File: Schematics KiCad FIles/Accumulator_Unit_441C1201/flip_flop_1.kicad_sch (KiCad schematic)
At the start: 13 parts, among them U1201 5963

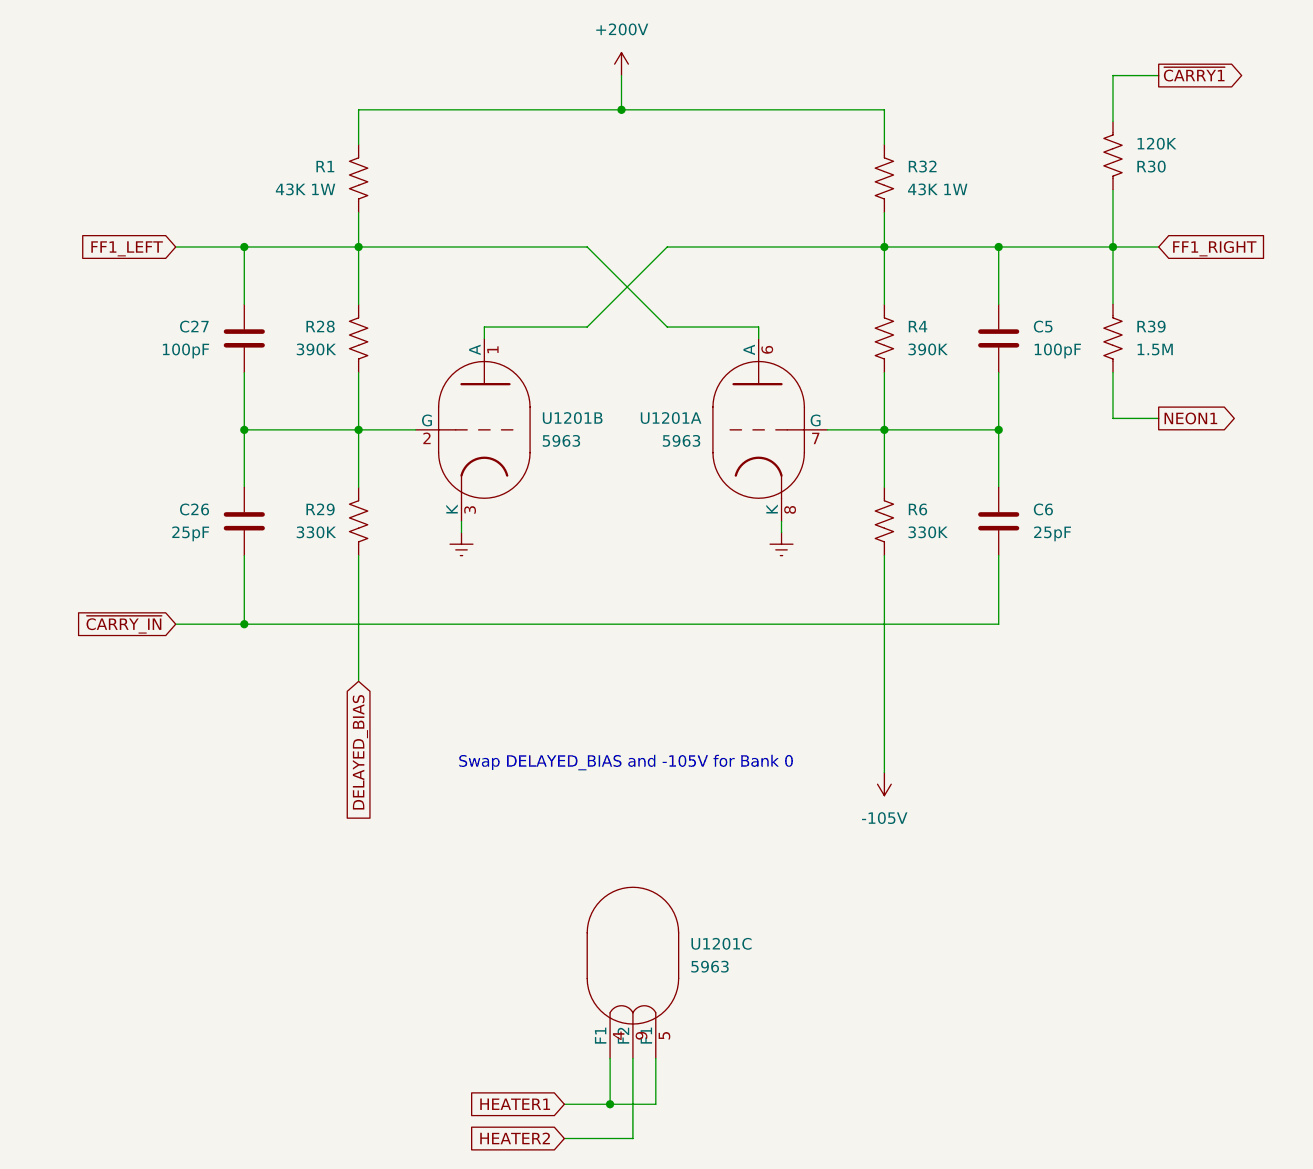
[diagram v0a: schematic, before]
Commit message: Fix component designators on accumulator schematics
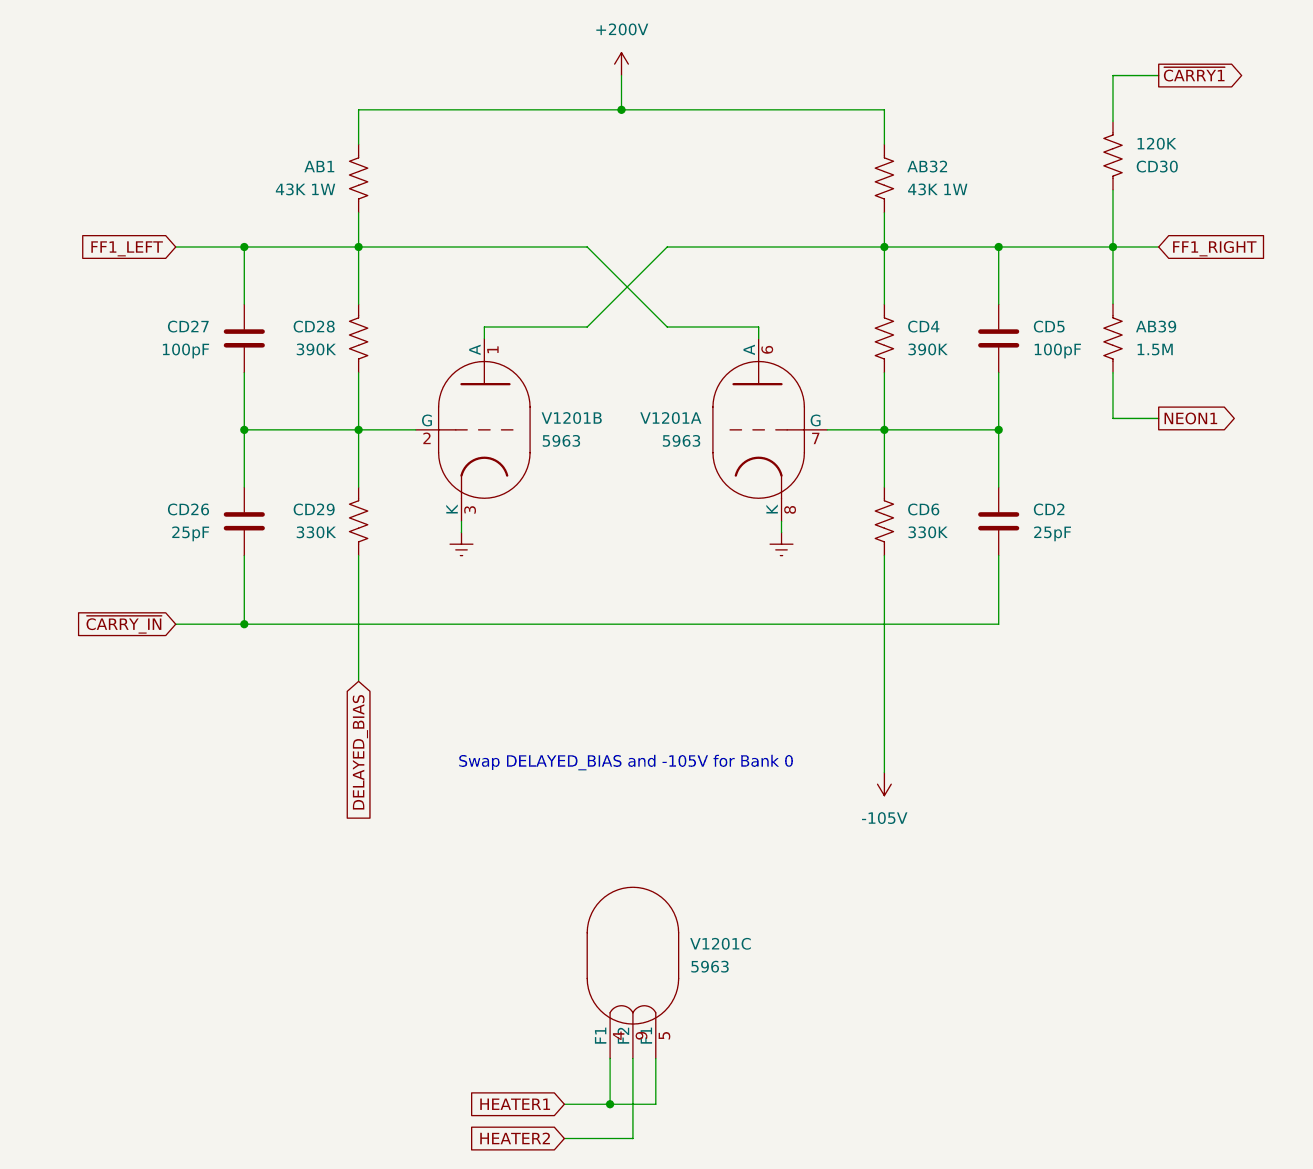
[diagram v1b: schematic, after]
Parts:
- renumbered R1 to AB1, R32 to AB32, R39 to AB39, C6 to CD2, C26 to CD26, C27 to CD27, R28 to CD28, R29 to CD29, R30 to CD30, R4 to CD4, C5 to CD5, R6 to CD6, U1201 to V1201
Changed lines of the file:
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@@
 		(on_board yes)
 		(dnp no)
-		(property "Reference" "R6"
+		(property "Reference" "CD6"
 			(at 171.45 85.0899 0)
 			(effects
@@
 			(project "Accumulator_Unit_441C1201"
 				(path "/519d7692-6bf3-45ab-bd58-713783b63e8a/fb897285-36a2-4bc7-a001-c032ab62393f"
-					(reference "R6")
+					(reference "CD6")
 					(unit 1)
 				)
@@
 		(on_board yes)
 		(dnp no)
-		(property "Reference" "R4"
+		(property "Reference" "CD4"
 			(at 171.45 64.7699 0)
 			(effects
@@
 			(project "Accumulator_Unit_441C1201"
 				(path "/519d7692-6bf3-45ab-bd58-713783b63e8a/fb897285-36a2-4bc7-a001-c032ab62393f"
-					(reference "R4")
+					(reference "CD4")
 					(unit 1)
 				)
@@
 		(on_board yes)
 		(dnp no)
-		(property "Reference" "R29"
+		(property "Reference" "CD29"
 			(at 107.95 85.0899 0)
 			(effects
@@
 			(project "Accumulator_Unit_441C1201"
 				(path "/519d7692-6bf3-45ab-bd58-713783b63e8a/fb897285-36a2-4bc7-a001-c032ab62393f"
-					(reference "R29")
+					(reference "CD29")
 					(unit 1)
 				)
@@
 		(on_board yes)
 		(dnp no)
-		(property "Reference" "U1201"
+		(property "Reference" "V1201"
 			(at 148.59 74.9299 0)
 			(effects
@@
 			(project "Accumulator_Unit_441C1201"
 				(path "/519d7692-6bf3-45ab-bd58-713783b63e8a/fb897285-36a2-4bc7-a001-c032ab62393f"
-					(reference "U1201")
+					(reference "V1201")
 					(unit 1)
 				)
@@
 		(on_board yes)
 		(dnp no)
-		(property "Reference" "C26"
+		(property "Reference" "CD26"
 			(at 93.98 85.0899 0)
 			(effects
@@
 			(project "Accumulator_Unit_441C1201"
 				(path "/519d7692-6bf3-45ab-bd58-713783b63e8a/fb897285-36a2-4bc7-a001-c032ab62393f"
-					(reference "C26")
+					(reference "CD26")
 					(unit 1)
 				)
@@
 		(on_board yes)
 		(dnp no)
-		(property "Reference" "R28"
+		(property "Reference" "CD28"
 			(at 107.95 64.7699 0)
 			(effects
@@
 			(project "Accumulator_Unit_441C1201"
 				(path "/519d7692-6bf3-45ab-bd58-713783b63e8a/fb897285-36a2-4bc7-a001-c032ab62393f"
-					(reference "R28")
+					(reference "CD28")
 					(unit 1)
 				)
@@
 		(on_board yes)
 		(dnp no)
-		(property "Reference" "R32"
+		(property "Reference" "AB32"
 			(at 171.45 46.9899 0)
 			(effects
@@
 			(project "Accumulator_Unit_441C1201"
 				(path "/519d7692-6bf3-45ab-bd58-713783b63e8a/fb897285-36a2-4bc7-a001-c032ab62393f"
-					(reference "R32")
+					(reference "AB32")
 					(unit 1)
 				)
@@
 		(dnp no)
 		(fields_autoplaced yes)
-		(property "Reference" "U1201"
+		(property "Reference" "V1201"
 			(at 147.32 133.3499 0)
 			(effects
@@
 			(project "Accumulator_Unit_441C1201"
 				(path "/519d7692-6bf3-45ab-bd58-713783b63e8a/fb897285-36a2-4bc7-a001-c032ab62393f"
-					(reference "U1201")
+					(reference "V1201")
 					(unit 3)
 				)
@@
 		(on_board yes)
 		(dnp no)
-		(property "Reference" "C5"
+		(property "Reference" "CD5"
 			(at 185.42 64.7699 0)
 			(effects
@@
 			(project "Accumulator_Unit_441C1201"
 				(path "/519d7692-6bf3-45ab-bd58-713783b63e8a/fb897285-36a2-4bc7-a001-c032ab62393f"
-					(reference "C5")
+					(reference "CD5")
 					(unit 1)
 				)
@@
 		(on_board yes)
 		(dnp no)
-		(property "Reference" "R30"
+		(property "Reference" "CD30"
 			(at 196.85 46.9901 0)
 			(effects
@@
 			(project "Accumulator_Unit_441C1201"
 				(path "/519d7692-6bf3-45ab-bd58-713783b63e8a/fb897285-36a2-4bc7-a001-c032ab62393f"
-					(reference "R30")
+					(reference "CD30")
 					(unit 1)
 				)
@@
 		(on_board yes)
 		(dnp no)
-		(property "Reference" "C27"
+		(property "Reference" "CD27"
 			(at 93.98 64.7699 0)
 			(effects
@@
 			(project "Accumulator_Unit_441C1201"
 				(path "/519d7692-6bf3-45ab-bd58-713783b63e8a/fb897285-36a2-4bc7-a001-c032ab62393f"
-					(reference "C27")
+					(reference "CD27")
 					(unit 1)
 				)
@@
 		(on_board yes)
 		(dnp no)
-		(property "Reference" "C6"
+		(property "Reference" "CD2"
 			(at 185.42 85.0899 0)
 			(effects
@@
 			(project "Accumulator_Unit_441C1201"
 				(path "/519d7692-6bf3-45ab-bd58-713783b63e8a/fb897285-36a2-4bc7-a001-c032ab62393f"
-					(reference "C6")
+					(reference "CD2")
 					(unit 1)
 				)
@@
 		(dnp no)
 		(fields_autoplaced yes)
-		(property "Reference" "U1201"
+		(property "Reference" "V1201"
 			(at 130.81 74.9299 0)
 			(effects
@@
 			(project "Accumulator_Unit_441C1201"
 				(path "/519d7692-6bf3-45ab-bd58-713783b63e8a/fb897285-36a2-4bc7-a001-c032ab62393f"
-					(reference "U1201")
+					(reference "V1201")
 					(unit 2)
 				)
@@
 		(on_board yes)
 		(dnp no)
-		(property "Reference" "R39"
+		(property "Reference" "AB39"
 			(at 196.85 64.7699 0)
 			(effects
@@
 			(project "Accumulator_Unit_441C1201"
 				(path "/519d7692-6bf3-45ab-bd58-713783b63e8a/fb897285-36a2-4bc7-a001-c032ab62393f"
-					(reference "R39")
+					(reference "AB39")
 					(unit 1)
 				)
@@
 		(on_board yes)
 		(dnp no)
-		(property "Reference" "R1"
+		(property "Reference" "AB1"
 			(at 107.95 46.9899 0)
 			(effects
@@
 			(project "Accumulator_Unit_441C1201"
 				(path "/519d7692-6bf3-45ab-bd58-713783b63e8a/fb897285-36a2-4bc7-a001-c032ab62393f"
-					(reference "R1")
-					(unit 1)
-				)
+					(reference "AB1")
+					(unit 1)
+				)
